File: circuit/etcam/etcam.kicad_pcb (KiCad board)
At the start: 2 copper layers, 100 x 50 mm, 86 parts, among them J1 SWD_connector, J2 USB_connector, J3 ESC_signal_connector, J4 ESC_GND_connector, J5 MCU_PWR_SRC_selector, J6 jumper_park, SW1 reset_SW, U1 FT232RL, U2 Si8640BB-B-IS1, U3 Si8640BB-B-IS1, U4 Si8640BB-B-IS1, U5 Si8640BB-B-IS1, U6 74HC251, U7 STM32F303xD/E-LQFP64, U8 LM1117-3.3, U9 ADuM5020, Y1 8MHz

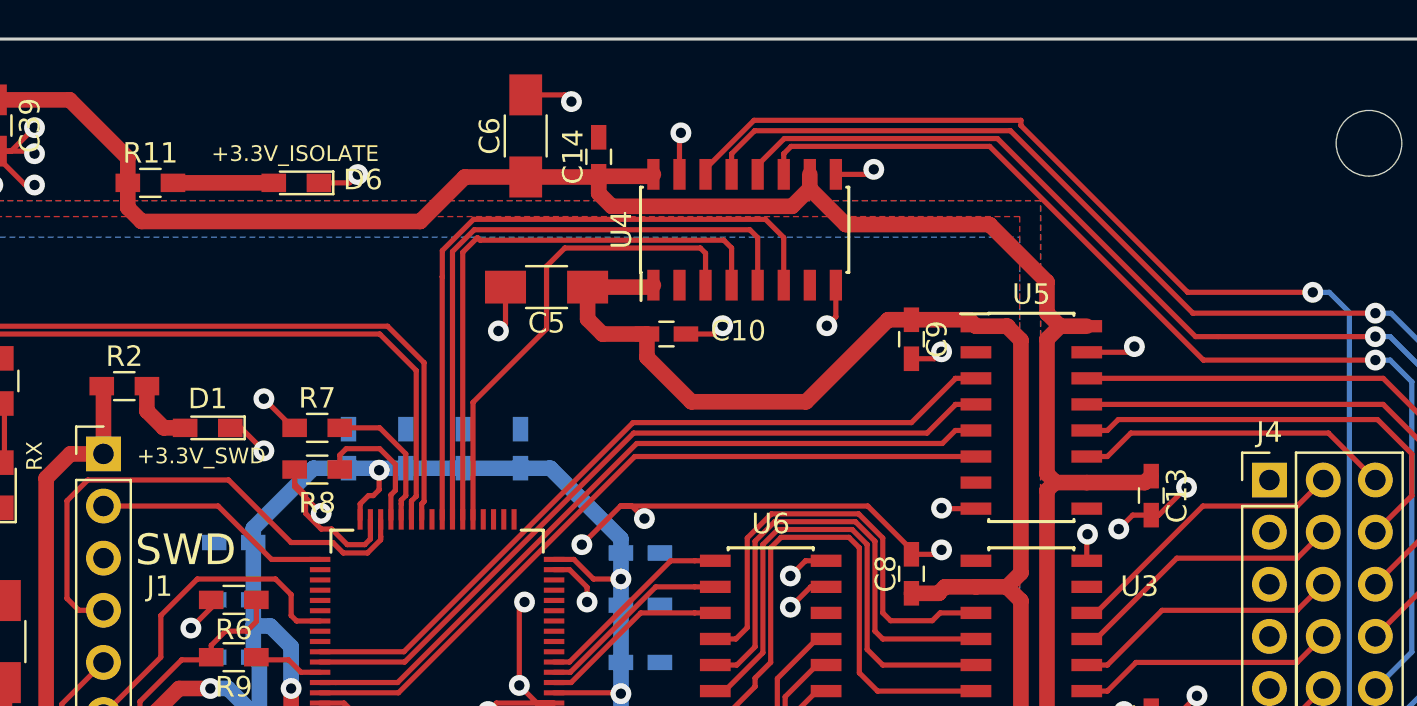
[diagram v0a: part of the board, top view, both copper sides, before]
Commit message: added ETCAM description into PCB
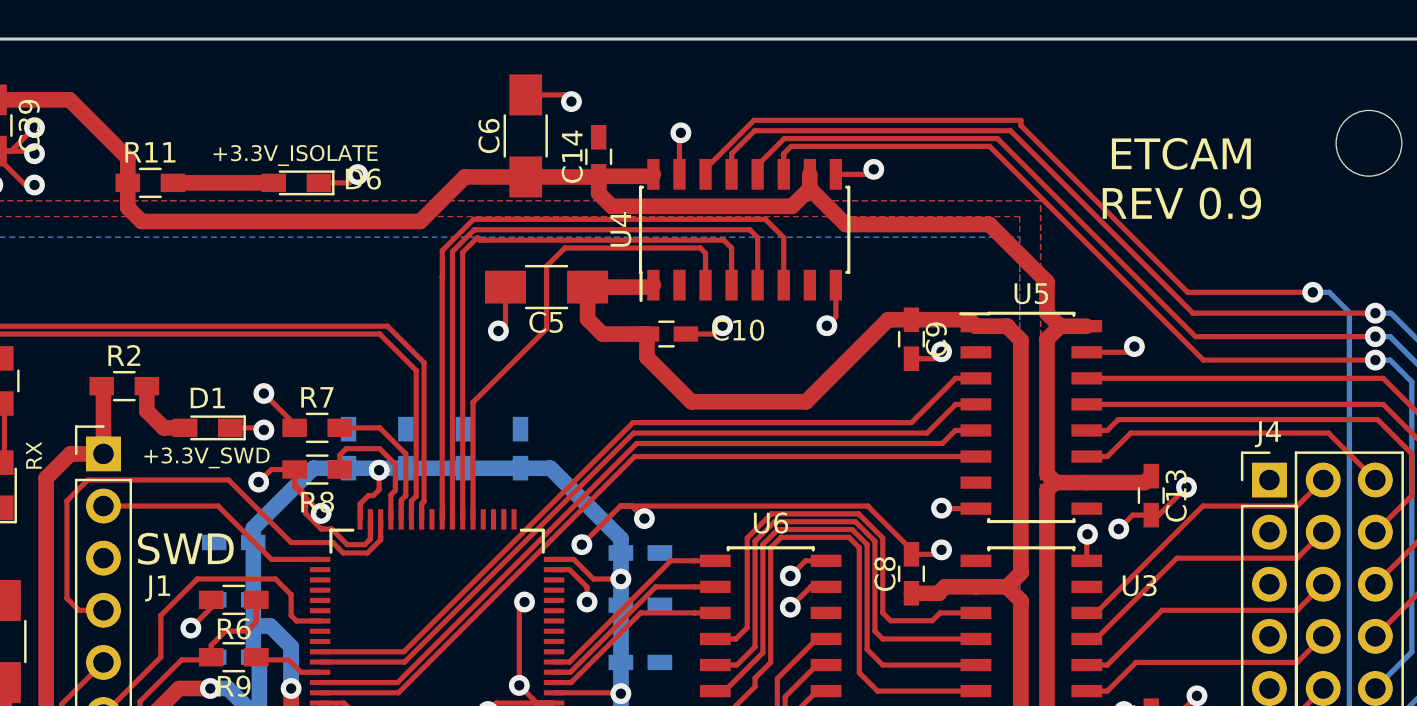
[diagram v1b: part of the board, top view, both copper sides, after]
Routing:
- net GND: track 143.8 -> 145.6 mm, vias 44 -> 45
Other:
- board text added: "ETCAM REV 0.9"
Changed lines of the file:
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@@
     (area 92.830999 67.084999 192.981001 117.235001)
     (thickness 1.6)
-    (drawings 36)
-    (tracks 904)
+    (drawings 37)
+    (tracks 907)
     (zones 0)
     (modules 86)
@@
   )
   (setup
-    (last_trace_width 0.762)
+    (last_trace_width 0.254)
     (user_trace_width 0.508)
     (user_trace_width 0.762)
@@
       (outputformat 1)
       (mirror false)
-      (drillshape 1)
+      (drillshape 0)
       (scaleselection 1)
       (outputdirectory ""))
@@
       (effects (font (size 1 1) (thickness 0.15)))
     )
-    (fp_text value +3.3V_SWD_LED (at 0 1.55 180) (layer F.Fab)
+    (fp_text value +3.3V_SWD_LED (at -3.752 1.55 180) (layer F.Fab)
       (effects (font (size 1 1) (thickness 0.15)))
     )
@@
     (pad 1 np_thru_hole circle (at 0 0) (size 3.2 3.2) (drill 3.2) (layers *.Cu *.Mask))
   )
+  (gr_text "ETCAM\nREV 0.9" (at 179.012 74.018) (layer F.SilkS)
+    (effects (font (size 1.5 1.5) (thickness 0.3)))
+  )
   (gr_text RX (at 123.132 87.48 90) (layer F.SilkS)
     (effects (font (size 0.762 0.762) (thickness 0.1905)))
@@
     (effects (font (size 0.762 0.762) (thickness 0.1905)))
   )
-  (gr_text +3.3V_SWD (at 131.26 87.48) (layer F.SilkS)
+  (gr_text +3.3V_SWD (at 131.514 87.48) (layer F.SilkS)
     (effects (font (size 0.762 0.762) (thickness 0.1905)))
   )
@@
     (effects (font (size 0.762 0.762) (thickness 0.1905)))
   )
-  (gr_text SWD (at 130.498 92.052 360) (layer F.SilkS)
+  (gr_text SWD (at 130.498 92.052) (layer F.SilkS)
     (effects (font (size 1.5 1.5) (thickness 0.3)))
   )
@@
   (segment (start 106.92 108.356) (end 106.92 106.594) (width 0.762) (layer F.Cu) (net 1))
   (segment (start 106.92 106.594) (end 108.104 105.41) (width 0.762) (layer F.Cu) (net 1))
+  (segment (start 135.806 88.138) (end 134.666 88.138) (width 0.254) (layer F.Cu) (net 2))
+  (segment (start 134.666 88.138) (end 134.054 88.75) (width 0.254) (layer F.Cu) (net 2))
+  (via (at 134.054 88.75) (size 1.016) (drill 0.5) (layers F.Cu B.Cu) (net 2))
+  (segment (start 132.672 86.106) (end 134.204 86.106) (width 0.254) (layer F.Cu) (net 2))
+  (segment (start 134.204 86.106) (end 134.308 86.21) (width 0.254) (layer F.Cu) (net 2))
+  (via (at 134.308 86.21) (size 1.016) (drill 0.5) (layers F.Cu B.Cu) (net 2))
+  (segment (start 135.806 86.106) (end 135.806 85.93) (width 0.254) (layer F.Cu) (net 2))
+  (segment (start 135.806 85.93) (end 134.308 84.432) (width 0.254) (layer F.Cu) (net 2))
+  (via (at 134.308 84.432) (size 1.016) (drill 0.5) (layers F.Cu B.Cu) (net 2))
   (segment (start 102.05 84.316) (end 102.05 84.686) (width 0.762) (layer F.Cu) (net 2))
   (segment (start 102.05 84.686) (end 102.812 85.448) (width 0.762) (layer F.Cu) (net 2))
@@
   (segment (start 131.742 94.872) (end 130.752 95.862) (width 0.254) (layer F.Cu) (net 2))
   (via (at 130.752 95.862) (size 1.016) (drill 0.5) (layers F.Cu B.Cu) (net 2))
-  (segment (start 135.806 86.106) (end 135.728 86.106) (width 0.254) (layer F.Cu) (net 2))
-  (via (at 134.308 84.686) (size 1.016) (drill 0.5) (layers F.Cu B.Cu) (net 2))
-  (segment (start 135.728 86.106) (end 134.308 84.686) (width 0.254) (layer F.Cu) (net 2))
   (segment (start 146.082 79.248) (end 146.082 81.04) (width 0.254) (layer F.Cu) (net 2))
   (segment (start 146.082 81.04) (end 145.738 81.384) (width 0.254) (layer F.Cu) (net 2))
@@
   (segment (start 135.806 88.138) (end 135.806 88.842) (width 0.254) (layer F.Cu) (net 2))
   (segment (start 135.806 88.842) (end 136.34 89.376) (width 0.254) (layer F.Cu) (net 2))
-  (segment (start 132.672 86.106) (end 133.188 86.106) (width 0.254) (layer F.Cu) (net 2))
-  (segment (start 133.188 86.106) (end 134.308 87.226) (width 0.254) (layer F.Cu) (net 2))
-  (via (at 134.308 87.226) (size 1.016) (drill 0.5) (layers F.Cu B.Cu) (net 2))
   (segment (start 117.348 95.57) (end 118.598 95.57) (width 0.254) (layer F.Cu) (net 2))
   (segment (start 118.598 95.57) (end 119.322 94.846) (width 0.254) (layer F.Cu) (net 2))

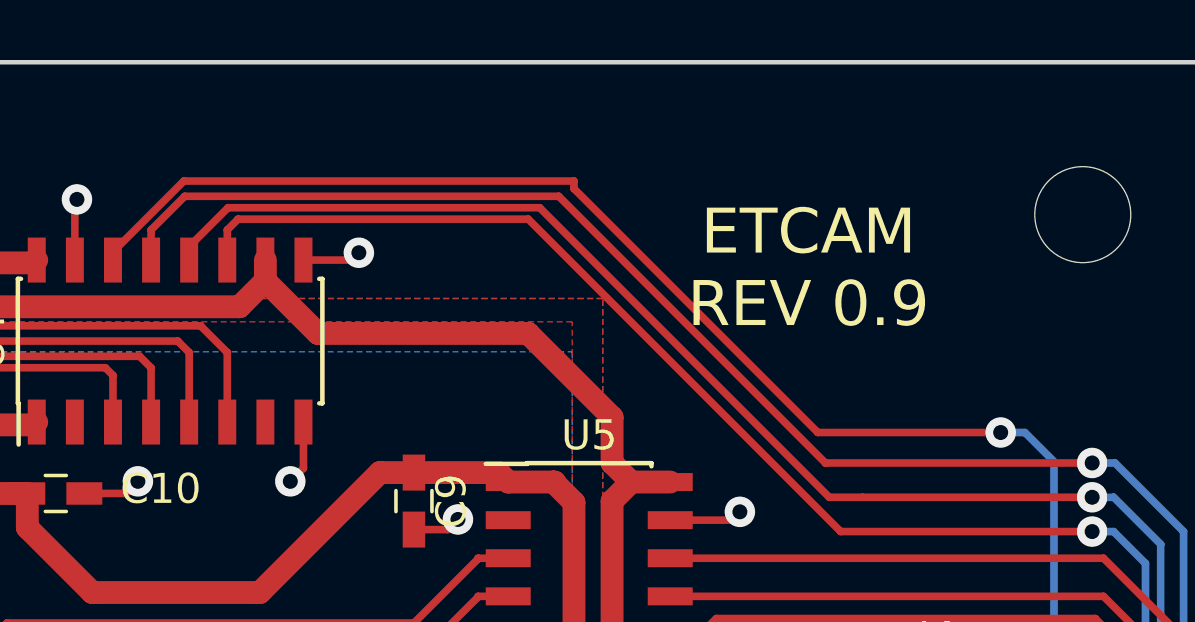
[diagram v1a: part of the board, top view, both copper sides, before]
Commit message: fixed straight trace in ETCAM PCB
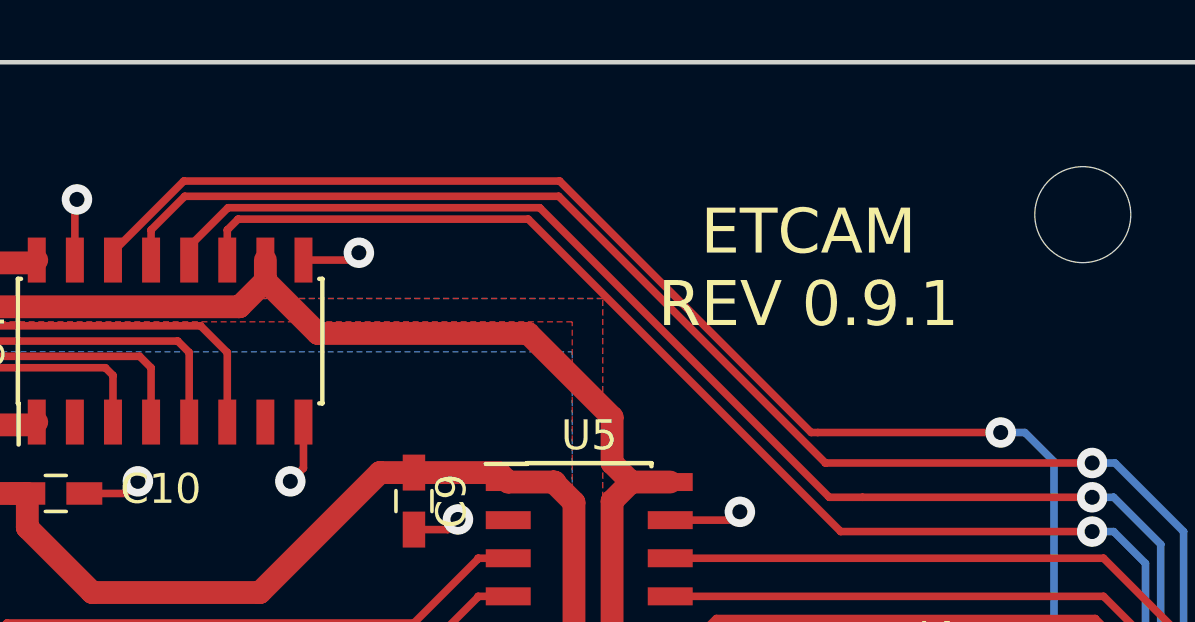
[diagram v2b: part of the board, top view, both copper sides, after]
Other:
- board text added: "ETCAM REV 0.9.1"
- board text removed: "ETCAM REV 0.9"
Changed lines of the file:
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@@
     (links 243)
     (no_connects 0)
-    (area 92.830999 67.084999 192.981001 117.235001)
+    (area 87.231857 65.868 204.763277 124.620001)
     (thickness 1.6)
     (drawings 37)
@@
     (title Embedded_Thruster_Control_And_Monitor_system)
     (date 2019-04-20)
-    (rev 0.9.0)
+    (rev 0.9.1)
   )
   (layers
@@
     (pad 1 np_thru_hole circle (at 0 0) (size 3.2 3.2) (drill 3.2) (layers *.Cu *.Mask))
   )
-  (gr_text "ETCAM\nREV 0.9" (at 179.012 74.018) (layer F.SilkS)
+  (gr_text "ETCAM\nREV 0.9.1" (at 179.012 74.018) (layer F.SilkS)
     (effects (font (size 1.5 1.5) (thickness 0.3)))
   )
@@
   (segment (start 103.378 101.854) (end 103.378 97.79) (width 0.254) (layer F.Cu) (net 18))
   (segment (start 102.616 97.028) (end 100.59 97.028) (width 0.254) (layer F.Cu) (net 18))
+  (segment (start 158.190174 71.12) (end 170.718828 71.12) (width 0.254) (layer F.Cu) (net 19))
+  (segment (start 170.718828 71.12) (end 179.100828 79.502) (width 0.254) (layer F.Cu) (net 19))
+  (segment (start 179.100828 79.502) (end 179.324 79.502) (width 0.254) (layer F.Cu) (net 19))
   (segment (start 155.829 73.754) (end 155.829 73.481174) (width 0.254) (layer F.Cu) (net 19))
   (segment (start 155.829 73.481174) (end 158.190174 71.12) (width 0.254) (layer F.Cu) (net 19))
-  (segment (start 158.190174 71.12) (end 171.196 71.12) (width 0.254) (layer F.Cu) (net 19))
-  (segment (start 171.196 71.12) (end 171.196 71.374) (width 0.254) (layer F.Cu) (net 19))
-  (segment (start 171.196 71.374) (end 179.324 79.502) (width 0.254) (layer F.Cu) (net 19))
   (segment (start 179.324 79.502) (end 185.42 79.502) (width 0.254) (layer F.Cu) (net 19))
   (segment (start 185.42 79.502) (end 186.22558 79.502) (width 0.254) (layer B.Cu) (net 19))
